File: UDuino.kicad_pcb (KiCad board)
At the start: 2 copper layers, 108 parts, among them J101 Barrel_Jack, J102 PMOD1, J103 Conn_01x03_Male, J104 Conn_01x03_Male, J105 Conn_01x04_Male, J106 Conn_01x04_Male, J301 Screw_Terminal_01x04, Q901 TRANS_PNP-MMBT4403, Q902 TRANS_PNP-MMBT4403, Q903 TRANS_PNP-MMBT4403, Q904 TRANS_PNP-MMBT4403, U101 STM32L452VCTx, U1201 AP63205WU, U1301 AP63203WU, U301 DRV8833RTY, U401 NAU8315YG, U501 NAU8315YG

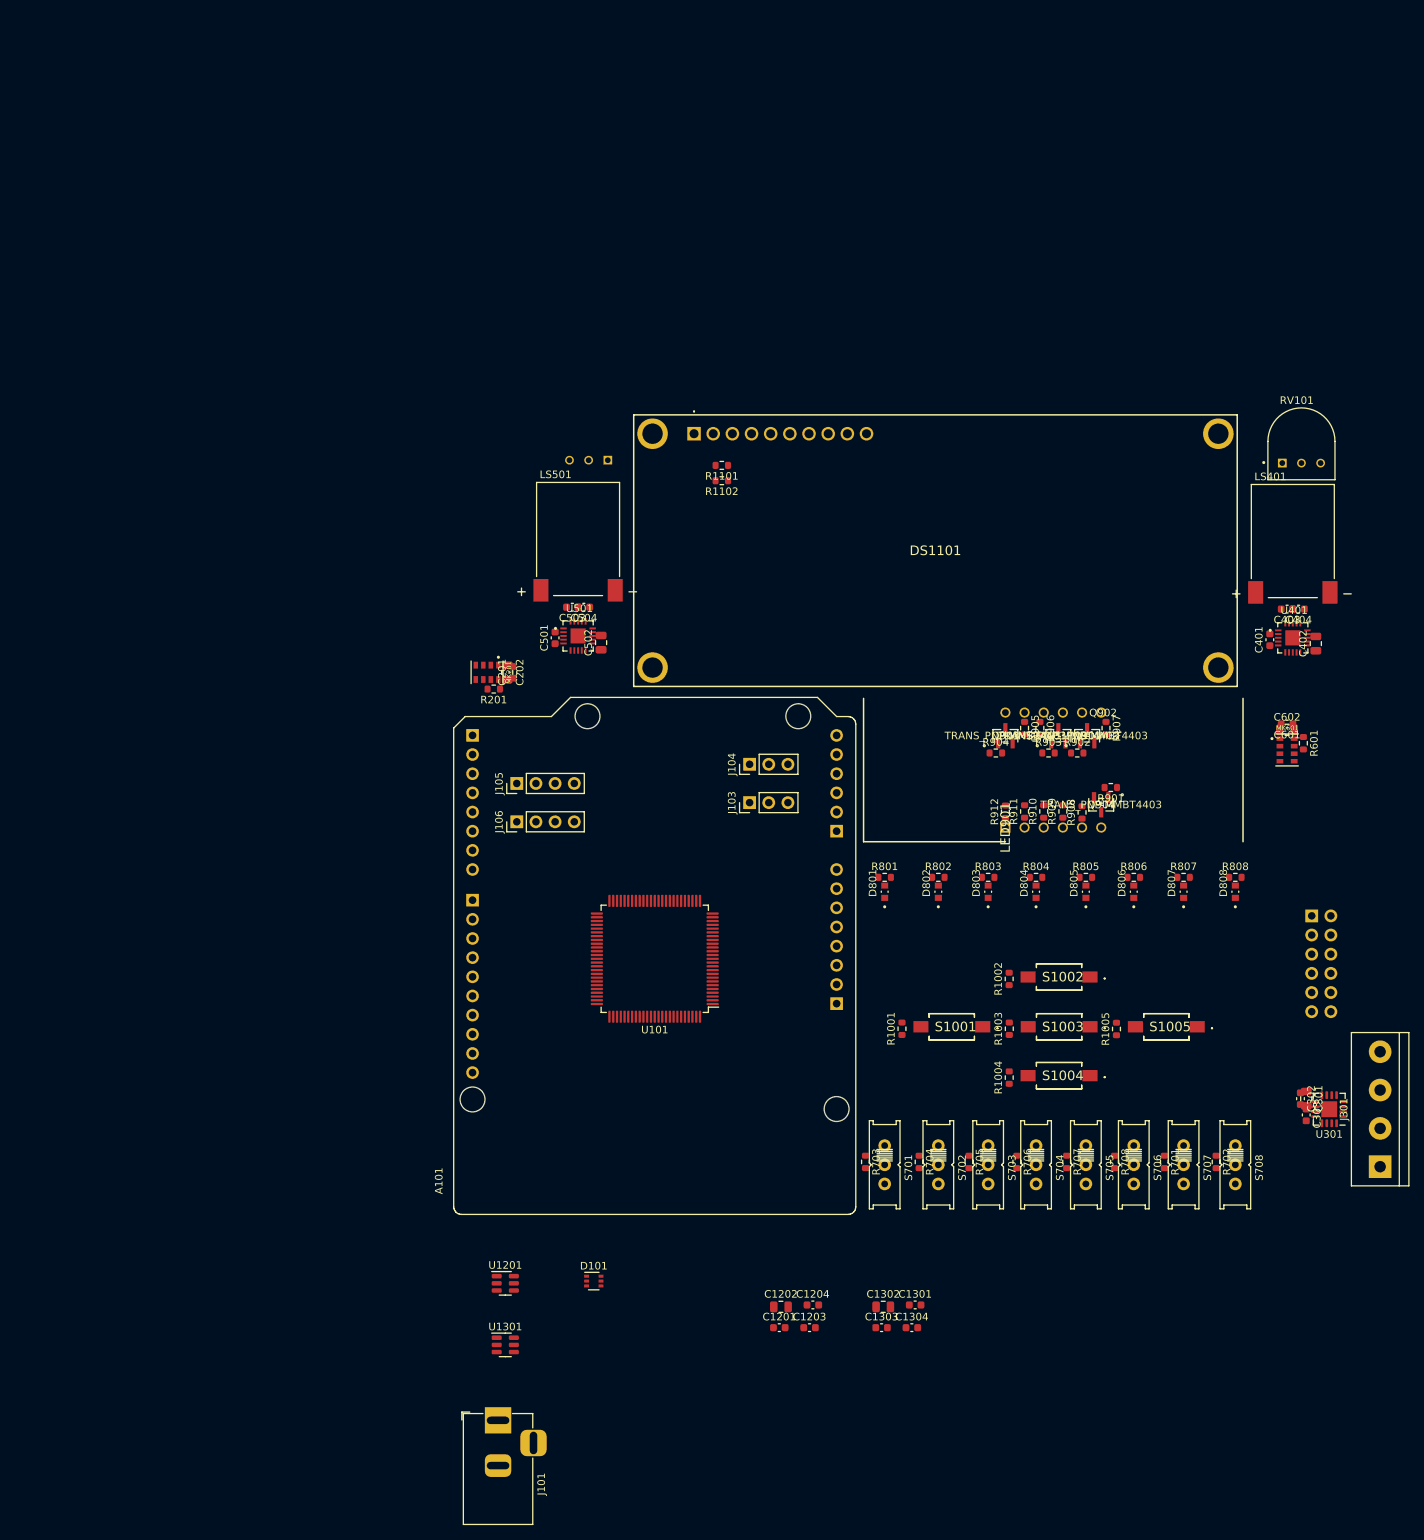
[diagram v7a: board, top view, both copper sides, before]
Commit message: Weekend progress
Things that remain:
4 LEDs to Microcontroller
7-Seg to Microcontroller
LCD to Microcontroller
Microphone and Speakers to Microcontroller
Power circuitry
USB-C connector
Reset and Boot buttons
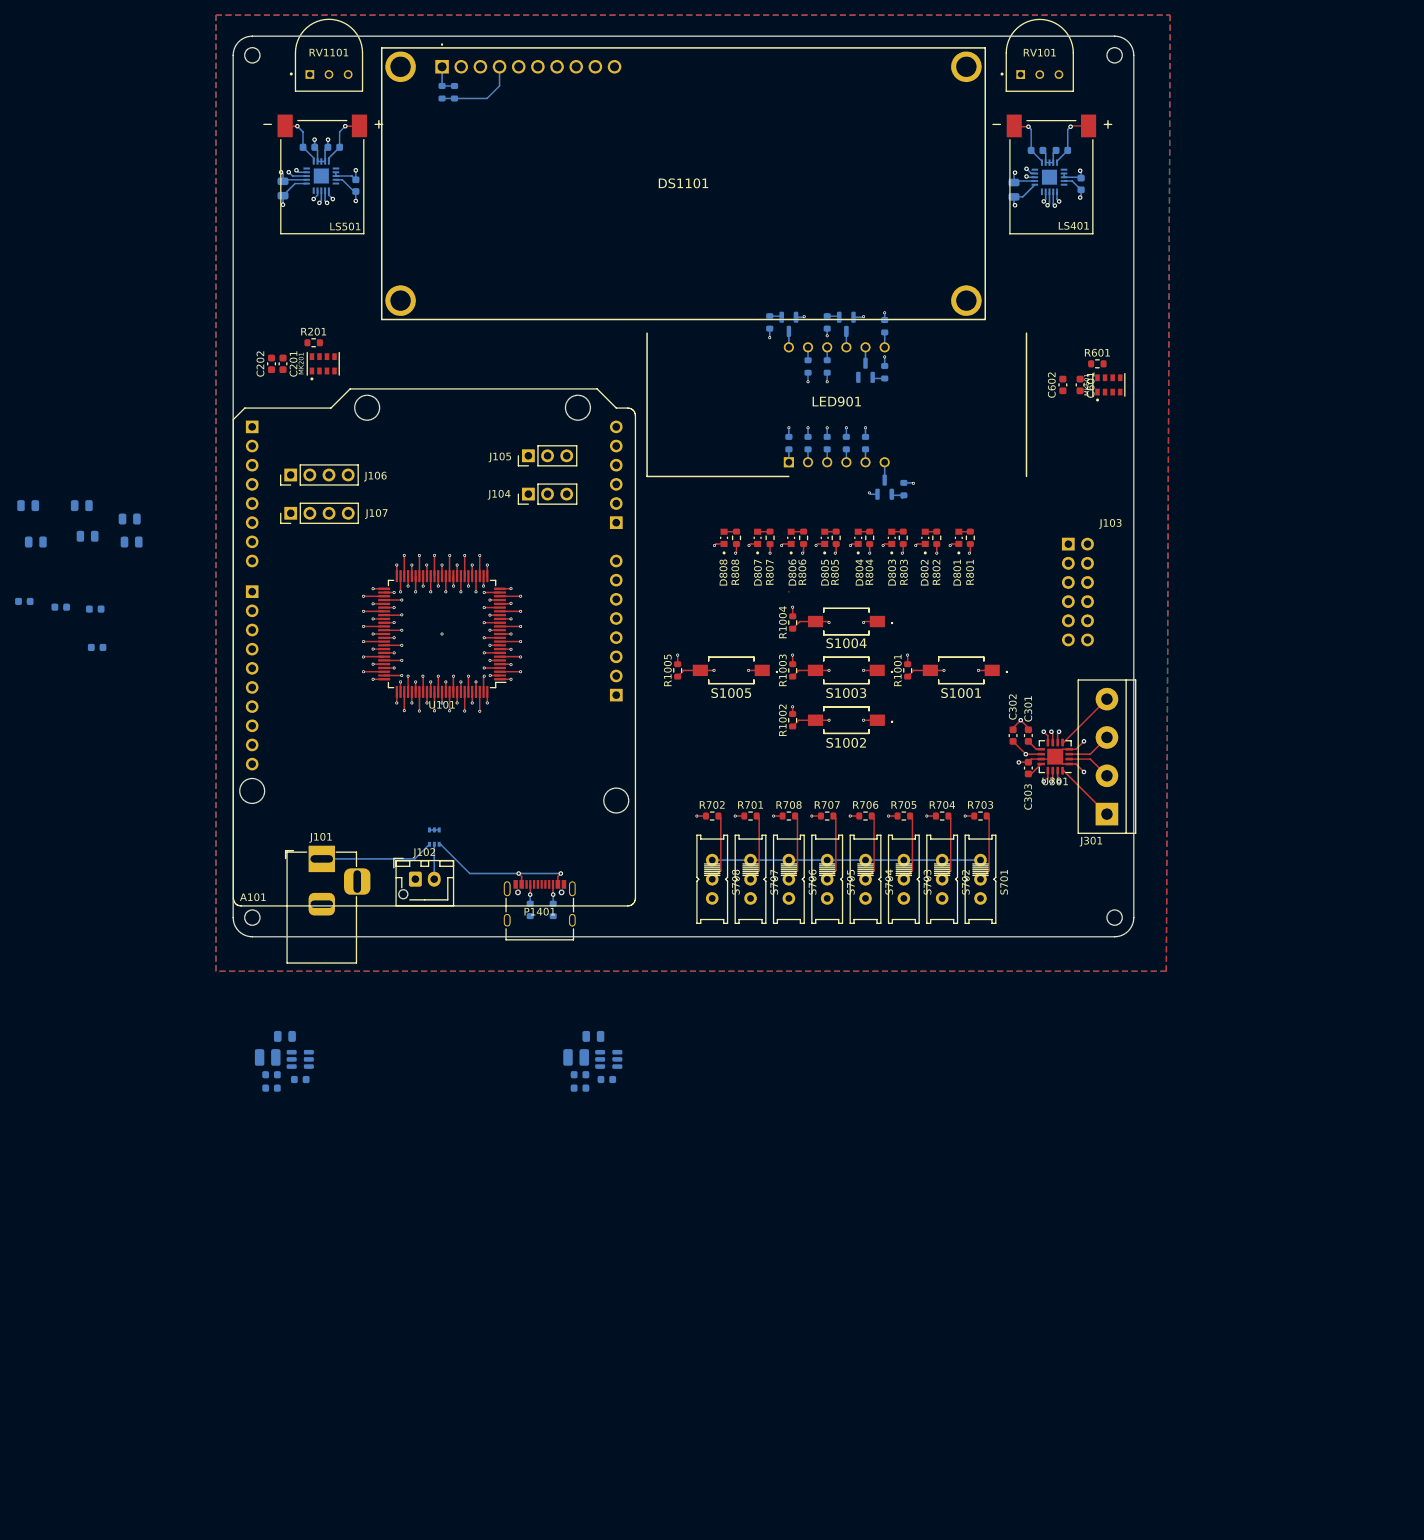
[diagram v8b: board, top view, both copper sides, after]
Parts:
- added C101: 100n, Capacitor_SMD:C_0805_2012Metric, B.Cu at (-26.2, 67.1)
- added C102: 100n, Capacitor_SMD:C_0805_2012Metric, B.Cu at (-19.3, 66.3)
- added C103: 100n, Capacitor_SMD:C_0805_2012Metric, B.Cu at (-20.1, 62.2)
- added C104: 100n, Capacitor_SMD:C_0805_2012Metric, B.Cu at (-13.7, 64.0)
- added C105: 100n, Capacitor_SMD:C_0805_2012Metric, B.Cu at (-27.2, 62.2)
- added C106: 4u7, Capacitor_SMD:C_0603_1608Metric, B.Cu at (-27.7, 74.9)
- added C107: 10n, Capacitor_SMD:C_0603_1608Metric, B.Cu at (-22.9, 75.7)
- added C108: 1u, Capacitor_SMD:C_0603_1608Metric, B.Cu at (-18.3, 75.9)
- added C109: 100n, Capacitor_SMD:C_0805_2012Metric, B.Cu at (-13.5, 67.1)
- added C110: 1u, Capacitor_SMD:C_0603_1608Metric, B.Cu at (-18.0, 81.0)
- added J102: Conn_01x02_Female, Connector_JST:JST_XH_B2B-XH-AM_1x02_P2.50mm_Vertical, F.Cu at (24.1, 111.7)
- added L1201: 4u7, Inductor_SMD:L_1008_2520Metric, B.Cu at (4.57, 135.4)
- added L1301: 4u7, Inductor_SMD:L_1008_2520Metric, B.Cu at (45.5, 135.4)
- added P1401: USB_C_Plug, Connector_USB:USB_C_Receptacle_Palconn_UTC16-G, F.Cu at (40.6, 114.9)
- added R1401: 5k1, Resistor_SMD:R_0603_1608Metric, B.Cu at (42.4, 115.8)
- added R1402: 5k1, Resistor_SMD:R_0603_1608Metric, B.Cu at (39.4, 115.8)
- C1201, C1202, C1203, C1204, C1301, C1302, C1303, C1304, C401, C402, C403, C404, C501, C502, C503, C504, D101, R1101, R1102, R901, R902, R903, R904, R905, R906, R907, R908, R909, R910, R911, R912, U1201, U1301, U401, U501: moved to B.Cu
- C202, C301, C602: footprint Capacitor_SMD:C_0805_2012Metric -> Capacitor_SMD:C_0603_1608Metric
- Q901, Q902, Q903, Q904: footprint Custom:MMBT4403LT3G -> Package_TO_SOT_SMD:SOT-23; moved to B.Cu
- RV1101: moved to F.Cu
- moved D808 82.4 mm to (65.1, 66.5)
- moved R702 81.0 mm to (63.5, 103.4), turned to 0 degrees
- moved R808 80.0 mm to (66.7, 66.5), turned to 90 degrees
- moved S708 79.0 mm to (63.5, 111.8)
- moved C1203 78.1 mm to (5.08, 139.4)
- moved J101 78.0 mm to (11.7, 109.1)
- moved C1204 78.0 mm to (5.08, 137.7)
- moved R1005 75.1 mm to (58.9, 84.1), turned to -90 degrees
- moved C1202 74.9 mm to (6.86, 132.6)
- moved S1005 74.5 mm to (66.0, 84.1)
- moved C502 73.5 mm to (6.60, 20.2)
- moved D807 73.4 mm to (69.5, 66.5)
- moved C402 72.3 mm to (103.5, 20.4)
- moved C1201 71.5 mm to (8.89, 138.3), turned to 180 degrees
- moved R701 71.5 mm to (68.6, 103.4), turned to 0 degrees
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- renumbered J102 to J103, J103 to J104, J104 to J105, J105 to J106, J106 to J107
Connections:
- net /7Seg/A renamed /7Seg-A
- net /7Seg/AN1 renamed /7Seg-AN1
- net /7Seg/AN2 renamed /7Seg-AN2
- net /7Seg/AN3 renamed /7Seg-AN3
- net /7Seg/AN4 renamed /7Seg-AN4
- net /7Seg/B renamed /7Seg-B
- net /7Seg/C renamed /7Seg-C
- net /7Seg/D renamed /7Seg-D
- net /7Seg/DP renamed /7Seg-DP
- net /7Seg/E renamed /7Seg-E
- net /7Seg/F renamed /7Seg-F
- net /7Seg/G renamed /7Seg-G
- net /Buttons/BT1 renamed /BTN1
- net /Buttons/BT2 renamed /BTN2
- net /Buttons/BT3 renamed /BTN3
- net /Buttons/BT4 renamed /BTN4
- net /Buttons/BT5 renamed /BTN5
- net /LCD/CSB renamed /LCD-NCSB
- net /LCD/RS renamed /LCD-RS
- net /LEDs/LED1 renamed /LED1
- net /LEDs/LED2 renamed /LED2
- net /LEDs/LED3 renamed /LED3
- net /LEDs/LED4 renamed /LED4
- net /LEDs/LED5 renamed /LED5
- net /LEDs/LED6 renamed /LED6
- net /LEDs/LED7 renamed /LED7
- net /LEDs/LED8 renamed /LED8
- net /Motor/AIN1 renamed /AIN1
- net /Motor/AIN2 renamed /AIN2
- net /Motor/BIN1 renamed /BIN1
- net /Motor/BIN2 renamed /BIN2
- net Net-(C1202-Pad1) renamed /Power 5V/SW
- net Net-(C1202-Pad2) renamed /Power 5V/BST
- net Net-(C1302-Pad1) renamed /Power 3V3/SW
- net Net-(C1302-Pad2) renamed /Power 3V3/BST
- A101 pad AREF: unconnected-(A101-PadAREF) -> +3V3
- A101 pad IOREF: unconnected-(A101-PadIOREF) -> +3V3
- A101 pad RST: unconnected-(A101-PadRST) -> /NRST
- C302 pad 2: +5V -> /V_IN
- D101 pad 2: /V_DC -> /V_BAT
- D101 pad 3: /V_BAT -> /V_DC
- J104 pad 2: +3V3 -> /V_IN
- J105 pad 2: +3V3 -> /V_IN
- Q901 pad 2: 5V -> +5V
- Q902 pad 2: 5V -> +5V
- Q903 pad 2: 5V -> +5V
- Q904 pad 2: 5V -> +5V
- R701 pad 1: /SW7 -> /SW2
- R702 pad 1: /SW8 -> /SW1
- R703 pad 1: /SW1 -> /SW8
- R704 pad 1: /SW2 -> /SW7
- R705 pad 1: /SW3 -> /SW6
- R706 pad 1: /SW4 -> /SW5
- R707 pad 1: /SW5 -> /SW4
- R708 pad 1: /SW6 -> /SW3
- RV1101 pad 1: +5V -> GND
- RV1101 pad 3: GND -> +5V
- U101 pad 14: unconnected-(U101-Pad14) -> /NRST
- U101 pad 20: unconnected-(U101-Pad20) -> GND
- U101 pad 21: unconnected-(U101-Pad21) -> +3V3
- U101 pad 6: +3V3 -> unconnected-(U101-Pad6)
- U101 pad 73: unconnected-(U101-Pad73) -> /V_USB
- U301 pad 10: +5V -> /V_IN
- U301 pad 15: /Motor/nSLEEP -> /D3
- U301 pad 6: /Motor/nFAULT -> /D2
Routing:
- net /BIN1: track 0.00 -> 90.3 mm, vias 0 -> 2
- net /BTN1: track 0.00 -> 87.9 mm, vias 0 -> 2
- net /AIN1: track 0.00 -> 87.6 mm, vias 0 -> 2
- net /LED1: track 0.00 -> 87.3 mm, vias 0 -> 2
- net /BIN2: track 0.00 -> 86.4 mm, vias 0 -> 2
- net /LED2: track 0.00 -> 86.3 mm, vias 0 -> 2
- net /AIN2: track 0.00 -> 82.8 mm, vias 0 -> 2
- net /SW8: track 0.00 -> 81.2 mm, vias 0 -> 2
- net /SW7: track 0.00 -> 80.9 mm, vias 0 -> 2
- net GND: track 0.00 -> 80.1 mm, vias 0 -> 33
- net +3V3: track 0.00 -> 78.3 mm, vias 0 -> 18
- net /LED3: track 0.00 -> 78.2 mm, vias 0 -> 2
- net /LED4: track 0.00 -> 76.4 mm, vias 0 -> 2
- net /SW6: track 0.00 -> 72.4 mm, vias 0 -> 2
- net /SW5: track 0.00 -> 70.7 mm, vias 0 -> 2
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- added copper zone on B.Cu, net GND
- added copper zone on F.Cu, net GND
- added copper zone on In1.Cu, net GND
- added copper zone on In2.Cu, net GND
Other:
- board outline added: 119.4 x 119.4 mm
- copper layers 2 -> 4
